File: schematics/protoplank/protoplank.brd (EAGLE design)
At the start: 80 x 49 mm, 112 parts, among them IC1 74AHC1G86DBV

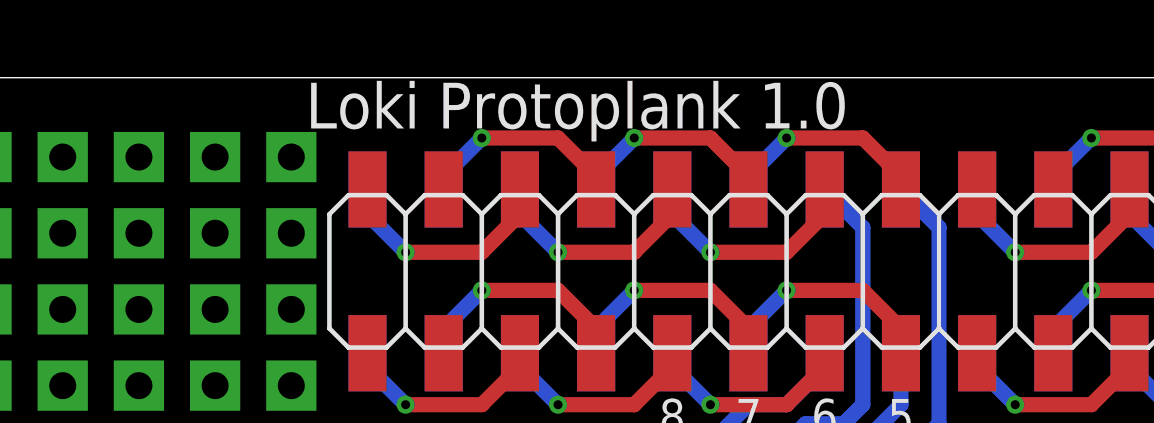
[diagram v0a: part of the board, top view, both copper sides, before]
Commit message: Tweaks to planks; change 0604 parts for 0805 where possible
Also added 4 pin plank; minor text changes.
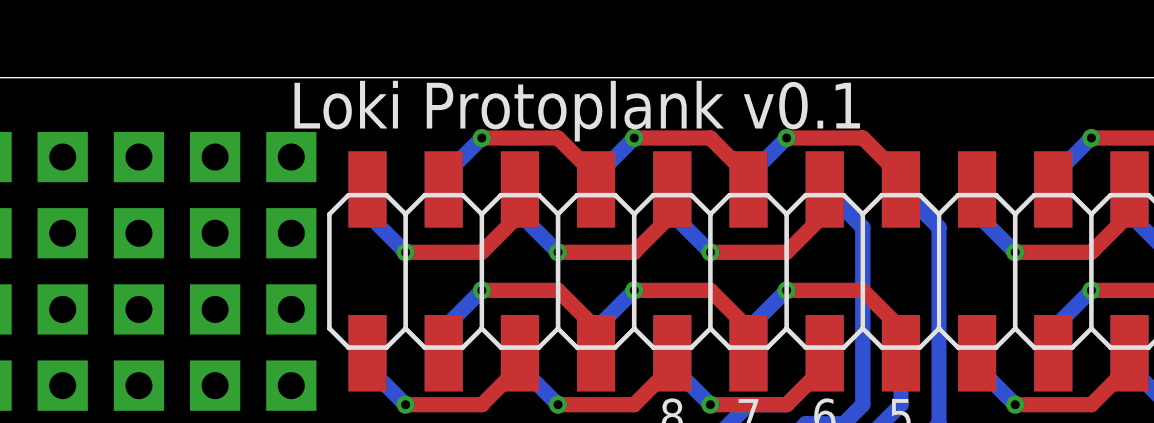
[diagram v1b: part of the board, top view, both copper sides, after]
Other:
- board text added: "Loki Protoplank v0.1"
- board text removed: "Loki Protoplank 1.0"
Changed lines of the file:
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@@
 <text x="52.07" y="9.8425" size="0.762" layer="21" rot="R180" align="bottom-center">+5v</text>
 <text x="49.53" y="9.8425" size="0.762" layer="21" rot="R180" align="bottom-center">VIN</text>
-<text x="41.275" y="47.3075" size="1.524" layer="21" align="bottom-center">Loki Protoplank 1.0</text>
+<text x="41.275" y="47.3075" size="1.524" layer="21" align="bottom-center">Loki Protoplank v0.1</text>
 <wire x1="2.8575" y1="7.3025" x2="9.8425" y2="7.3025" width="0.254" layer="21"/>
 <wire x1="9.8425" y1="7.3025" x2="9.8425" y2="9.2075" width="0.254" layer="21"/>

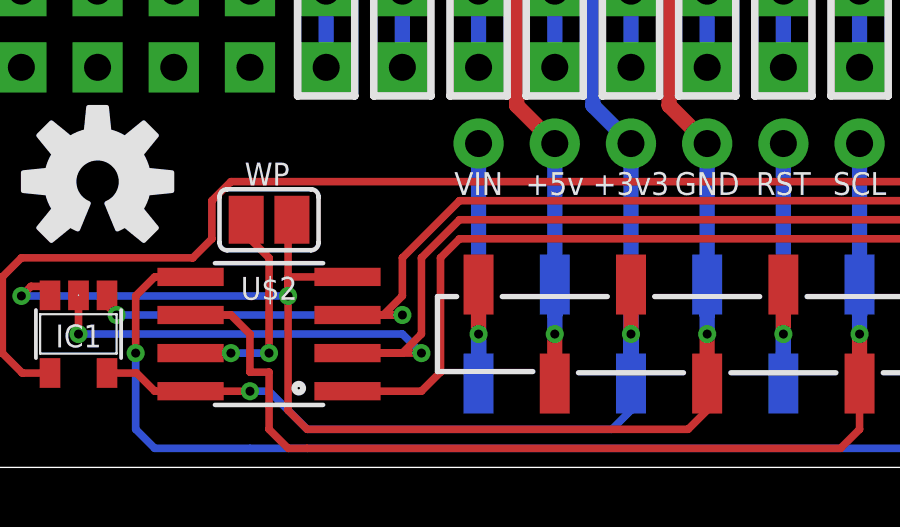
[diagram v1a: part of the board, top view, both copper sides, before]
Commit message: Fix write protect pullups on plank EEPROMs.
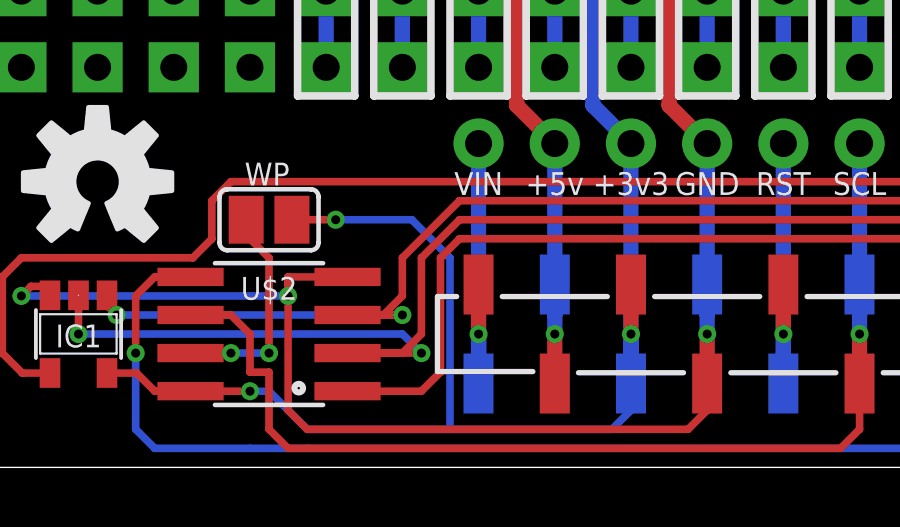
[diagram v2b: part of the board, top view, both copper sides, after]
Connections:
- net +3V3: now also WP.2
- net GND: no longer WP.2
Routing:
- net +3V3: track 87.2 -> 98.7 mm, vias 2 -> 3
- net GND: track 131.3 -> 128.7 mm
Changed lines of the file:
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@@
 <wire x1="41.91" y1="2.54" x2="42.545" y2="2.54" width="0.254" layer="16"/>
 <wire x1="42.545" y1="2.54" x2="43.815" y2="1.27" width="0.254" layer="16"/>
-<wire x1="43.815" y1="1.27" x2="53.975" y2="1.27" width="0.254" layer="16"/>
+<wire x1="43.815" y1="1.27" x2="48.5775" y2="1.27" width="0.254" layer="16"/>
+<wire x1="48.5775" y1="1.27" x2="53.975" y2="1.27" width="0.254" layer="16"/>
 <wire x1="53.975" y1="1.27" x2="54.61" y2="1.905" width="0.254" layer="16"/>
 <wire x1="54.61" y1="1.905" x2="54.61" y2="2.795" width="0.254" layer="16"/>
@@
 <contactref element="C1" pad="1"/>
 <wire x1="74.93" y1="38.4175" x2="74.93" y2="33.655" width="0.508" layer="16"/>
+<contactref element="WP" pad="2"/>
+<wire x1="43.307" y1="8.255" x2="44.7675" y2="8.255" width="0.254" layer="1"/>
+<via x="44.7675" y="8.255" extent="1-16" drill="0.3"/>
+<wire x1="44.7675" y1="8.255" x2="47.3075" y2="8.255" width="0.254" layer="16"/>
+<wire x1="47.3075" y1="8.255" x2="48.5775" y2="6.985" width="0.254" layer="16"/>
+<wire x1="48.5775" y1="6.985" x2="48.5775" y2="1.27" width="0.254" layer="16"/>
 </signal>
 <signal name="GND">
@@
 <contactref element="IC1" pad="3"/>
 <contactref element="U$2" pad="4"/>
-<contactref element="WP" pad="2"/>
 <contactref element="U$32" pad="P$2"/>
 <wire x1="57.15" y1="6.095" x2="57.15" y2="5.08" width="0.508" layer="16"/>
@@
 <wire x1="57.15" y1="1.905" x2="57.15" y2="2.795" width="0.254" layer="1"/>
 <wire x1="35.245" y1="5.735" x2="35.245" y2="6.035" width="0.254" layer="1"/>
-<wire x1="43.18" y1="8.89" x2="43.18" y2="8.382" width="0.254" layer="1"/>
-<wire x1="43.18" y1="8.382" x2="43.307" y2="8.255" width="0.254" layer="1"/>
 <wire x1="43.18" y1="5.715" x2="43.18" y2="6.35" width="0.254" layer="1"/>
-<wire x1="43.18" y1="6.35" x2="43.18" y2="8.128" width="0.254" layer="1"/>
-<wire x1="43.18" y1="8.128" x2="43.307" y2="8.255" width="0.254" layer="1"/>
+<wire x1="43.18" y1="6.35" x2="43.18" y2="8.128" width="0" layer="19" extent="1-16"/>
 <wire x1="45.1612" y1="6.35" x2="43.18" y2="6.35" width="0.254" layer="1"/>
 <wire x1="35.245" y1="6.035" x2="34.61" y2="6.035" width="0.254" layer="1"/>
